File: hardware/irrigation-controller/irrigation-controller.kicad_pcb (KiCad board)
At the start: 2 copper layers, 109 x 48.3 mm, 39 parts, among them J1 RS485, J12 RELAY_2, J3 I/O, J5 RF Module, J6 PWR 24V, J7 RELAY_1, J8 ESP32, J9 ESP32, U1 AQY280EH, U3 AQY280EH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

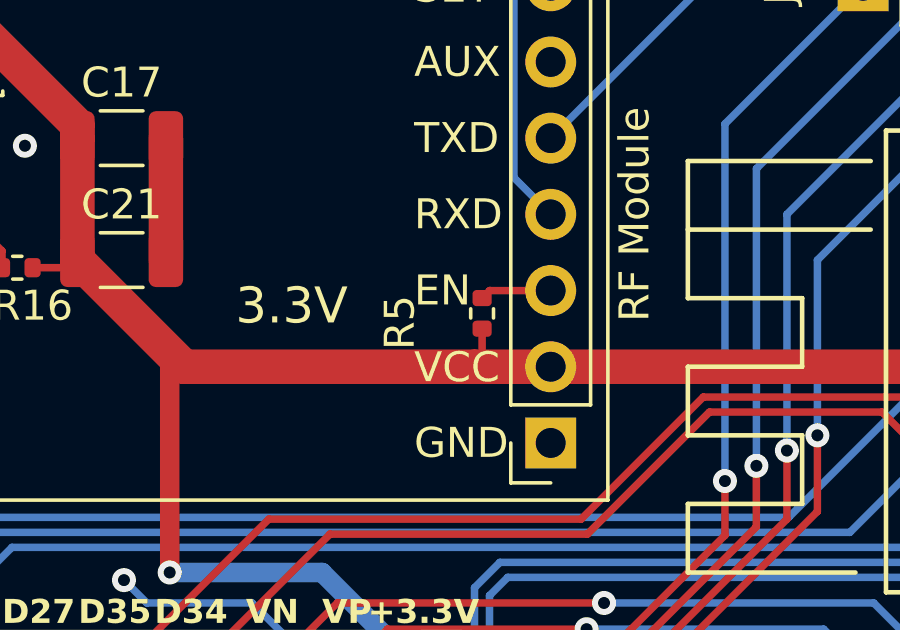
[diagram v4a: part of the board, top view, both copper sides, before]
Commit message: Fix for controller RF EN pin
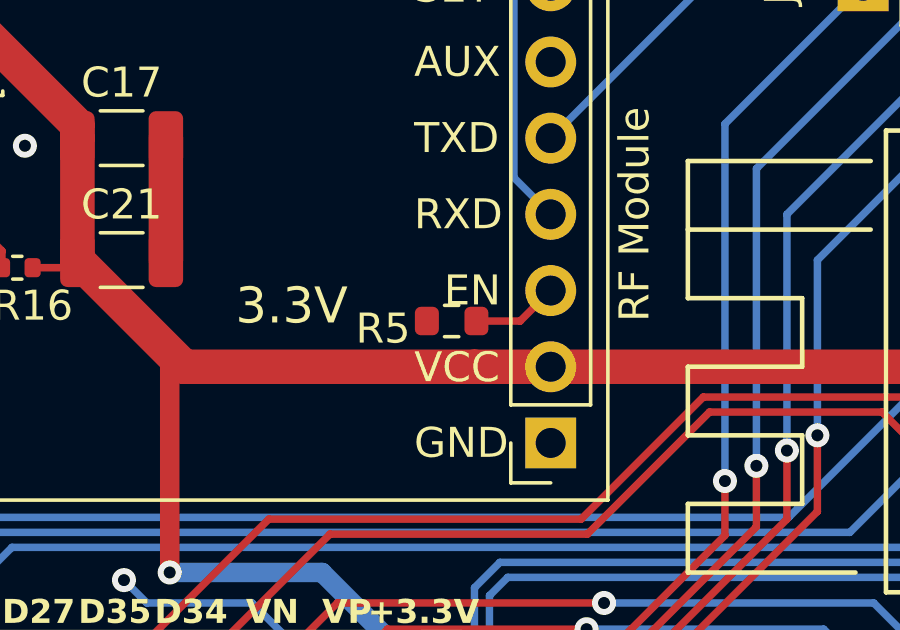
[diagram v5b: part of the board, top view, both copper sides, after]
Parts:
- R5: value 10k -> 3k; footprint Resistor_SMD:R_0402_1005Metric -> Resistor_SMD:R_0603_1608Metric
- moved R5 1.05 mm to (95.2, 92.5), turned to 180 degrees
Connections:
- R5 pad 2: +3.3V -> GND
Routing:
- net +3.3V: track 137.3 -> 135.9 mm
- net Net-(J5-Pin_3): track 2.39 -> 2.90 mm
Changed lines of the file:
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@@
         (effects (font (size 1 1) (thickness 0.15)) (justify left))
     )
-    (fp_text user "EN" (at 4.552 5.08 180) (layer "F.SilkS")
+    (fp_text user "EN" (at 3.556 5.08 180) (layer "F.SilkS")
         (effects (font (size 1 1) (thickness 0.15)) (justify left))
     )
@@
     )
   )
-  (footprint "Resistor_SMD:R_0402_1005Metric" (layer "F.Cu")
-    (at 96.266 92.202 -90)
-    (descr "Resistor SMD 0402 (1005 Metric), square (rectangular) end terminal, IPC_7351 nominal, (Body size source: IPC-SM-782 page 72, https://www.pcb-3d.com/wordpress/wp-content/uploads/ipc-sm-782a_amendment_1_and_2.pdf), generated with kicad-footprint-generator")
-    (tags "resistor")
-    (property "JLCPCB Basic" "")
-    (property "JLCPCB Part" "C25744")
-    (property "JLCPCB UP" "")
-    (property "Purchase Link" "NA")
-    (property "Sheetfile" "irrigation-controller.kicad_sch")
-    (property "Sheetname" "")
-    (property "ki_description" "Resistor")
-    (property "ki_keywords" "R res resistor")
-    (attr smd)
-    (fp_text reference "R5" (at 0.3048 2.7432 90) (layer "F.SilkS")
-        (effects (font (size 1 1) (thickness 0.15)))
-    )
-    (fp_text value "10k" (at 0 -1.395 90) (layer "F.Fab")
-        (effects (font (size 1 1) (thickness 0.15)))
-    )
-    (fp_text user "${REFERENCE}" (at 0 0 90) (layer "F.Fab")
-        (effects (font (size 0.26 0.26) (thickness 0.04)))
-    )
-    (fp_line (start -0.153641 -0.38) (end 0.153641 -0.38)
-      (stroke (width 0.12) (type solid)) (layer "F.SilkS"))
-    (fp_line (start -0.153641 0.38) (end 0.153641 0.38)
-      (stroke (width 0.12) (type solid)) (layer "F.SilkS"))
-    (fp_line (start -0.93 -0.47) (end 0.93 -0.47)
-      (stroke (width 0.05) (type solid)) (layer "F.CrtYd"))
-    (fp_line (start -0.93 0.47) (end -0.93 -0.47)
-      (stroke (width 0.05) (type solid)) (layer "F.CrtYd"))
-    (fp_line (start 0.93 -0.47) (end 0.93 0.47)
-      (stroke (width 0.05) (type solid)) (layer "F.CrtYd"))
-    (fp_line (start 0.93 0.47) (end -0.93 0.47)
-      (stroke (width 0.05) (type solid)) (layer "F.CrtYd"))
-    (fp_line (start -0.525 -0.27) (end 0.525 -0.27)
-      (stroke (width 0.1) (type solid)) (layer "F.Fab"))
-    (fp_line (start -0.525 0.27) (end -0.525 -0.27)
-      (stroke (width 0.1) (type solid)) (layer "F.Fab"))
-    (fp_line (start 0.525 -0.27) (end 0.525 0.27)
-      (stroke (width 0.1) (type solid)) (layer "F.Fab"))
-    (fp_line (start 0.525 0.27) (end -0.525 0.27)
-      (stroke (width 0.1) (type solid)) (layer "F.Fab"))
-    (pad "1" smd roundrect (at -0.51 0 270) (size 0.54 0.64) (layers "F.Cu" "F.Paste" "F.Mask") (roundrect_rratio 0.25)
-      (net 28 "Net-(J5-Pin_3)") (pintype "passive"))
-    (pad "2" smd roundrect (at 0.51 0 270) (size 0.54 0.64) (layers "F.Cu" "F.Paste" "F.Mask") (roundrect_rratio 0.25)
-      (net 7 "+3.3V") (pintype "passive"))
-    (model "${KISYS3DMOD}/Resistor_SMD.3dshapes/R_0402_1005Metric.wrl"
-      (offset (xyz 0 0 0))
-      (scale (xyz 1 1 1))
-      (rotate (xyz 0 0 0))
-    )
-  )
   (footprint "Resistor_SMD:R_0603_1608Metric" (layer "F.Cu")
     (at 75.17 91.44)
@@
     )
   )
+  (footprint "Resistor_SMD:R_0603_1608Metric" (layer "F.Cu")
+    (at 95.25 92.456 180)
+    (descr "Resistor SMD 0603 (1608 Metric), square (rectangular) end terminal, IPC_7351 nominal, (Body size source: IPC-SM-782 page 72, https://www.pcb-3d.com/wordpress/wp-content/uploads/ipc-sm-782a_amendment_1_and_2.pdf), generated with kicad-footprint-generator")
+    (tags "resistor")
+    (property "JLCPCB Part" "C4211")
+    (property "Purchase Link" "NA")
+    (property "Sheetfile" "irrigation-controller.kicad_sch")
+    (property "Sheetname" "")
+    (property "ki_description" "Resistor")
+    (property "ki_keywords" "R res resistor")
+    (attr smd)
+    (fp_text reference "R5" (at 2.286 -0.254 180) (layer "F.SilkS")
+        (effects (font (size 1 1) (thickness 0.15)))
+    )
+    (fp_text value "3k" (at 1.778 1.27) (layer "F.Fab")
+        (effects (font (size 1 1) (thickness 0.15)))
+    )
+    (fp_text user "${REFERENCE}" (at 0 0) (layer "F.Fab")
+        (effects (font (size 0.4 0.4) (thickness 0.06)))
+    )
+    (fp_line (start -0.237258 -0.5225) (end 0.237258 -0.5225)
+      (stroke (width 0.12) (type solid)) (layer "F.SilkS"))
+    (fp_line (start -0.237258 0.5225) (end 0.237258 0.5225)
+      (stroke (width 0.12) (type solid)) (layer "F.SilkS"))
+    (fp_line (start -1.48 -0.73) (end 1.48 -0.73)
+      (stroke (width 0.05) (type solid)) (layer "F.CrtYd"))
+    (fp_line (start -1.48 0.73) (end -1.48 -0.73)
+      (stroke (width 0.05) (type solid)) (layer "F.CrtYd"))
+    (fp_line (start 1.48 -0.73) (end 1.48 0.73)
+      (stroke (width 0.05) (type solid)) (layer "F.CrtYd"))
+    (fp_line (start 1.48 0.73) (end -1.48 0.73)
+      (stroke (width 0.05) (type solid)) (layer "F.CrtYd"))
+    (fp_line (start -0.8 -0.4125) (end 0.8 -0.4125)
+      (stroke (width 0.1) (type solid)) (layer "F.Fab"))
+    (fp_line (start -0.8 0.4125) (end -0.8 -0.4125)
+      (stroke (width 0.1) (type solid)) (layer "F.Fab"))
+    (fp_line (start 0.8 -0.4125) (end 0.8 0.4125)
+      (stroke (width 0.1) (type solid)) (layer "F.Fab"))
+    (fp_line (start 0.8 0.4125) (end -0.8 0.4125)
+      (stroke (width 0.1) (type solid)) (layer "F.Fab"))
+    (pad "1" smd roundrect (at -0.825 0 180) (size 0.8 0.95) (layers "F.Cu" "F.Paste" "F.Mask") (roundrect_rratio 0.25)
+      (net 28 "Net-(J5-Pin_3)") (pintype "passive"))
+    (pad "2" smd roundrect (at 0.825 0 180) (size 0.8 0.95) (layers "F.Cu" "F.Paste" "F.Mask") (roundrect_rratio 0.25)
+      (net 1 "GND") (pintype "passive"))
+    (model "${KICAD6_3DMODEL_DIR}/Resistor_SMD.3dshapes/R_0603_1608Metric.wrl"
+      (offset (xyz 0 0 0))
+      (scale (xyz 1 1 1))
+      (rotate (xyz 0 0 0))
+    )
+  )
   (footprint "lib:avocado" (layer "F.Cu")
     (at 137.16 93.98)
@@
   (segment (start 86.755 121.045) (end 94.082107 121.045) (width 0.25) (layer "F.Cu") (net 7))
   (segment (start 131.826 93.98) (end 144.526 81.28) (width 1.15) (layer "F.Cu") (net 7))
-  (segment (start 96.266 93.726) (end 96.012 93.98) (width 0.25) (layer "F.Cu") (net 7))
-  (segment (start 96.266 92.712) (end 96.266 93.726) (width 0.25) (layer "F.Cu") (net 7))
   (segment (start 94.082107 121.045) (end 96.365553 118.761554) (width 0.25) (layer "F.Cu") (net 7))
   (segment (start 82.775 90.424) (end 82.775 86.36) (width 1.15) (layer "F.Cu") (net 7))
@@
   (segment (start 104.360497 85.885503) (end 108.966 81.28) (width 0.25) (layer "B.Cu") (net 27))
   (segment (start 104.360497 97.79) (end 104.360497 85.885503) (width 0.25) (layer "B.Cu") (net 27))
-  (segment (start 98.552 91.44) (end 96.518 91.44) (width 0.25) (layer "F.Cu") (net 28))
-  (segment (start 96.518 91.44) (end 96.266 91.692) (width 0.25) (layer "F.Cu") (net 28))
+  (segment (start 96.075 92.456) (end 97.536 92.456) (width 0.25) (layer "F.Cu") (net 28))
+  (segment (start 97.536 92.456) (end 98.552 91.44) (width 0.25) (layer "F.Cu") (net 28))
   (segment (start 144.240518 78.555) (end 99.499 78.555) (width 0.25) (layer "B.Cu") (net 29))
   (segment (start 146.296 80.610481) (end 144.240518 78.555) (width 0.25) (layer "B.Cu") (net 29))
